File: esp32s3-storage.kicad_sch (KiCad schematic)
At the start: 27 parts, among them J1 USB_C_Receptacle_USB2.0_14P, J2 Conn_01x02, J3 Micro_SD_Card, J4 Conn_01x08_Socket, J5 Conn_01x15_Pin, J6 Conn_01x02_Pin, J7 Conn_01x03_Pin, Q1 CJ3401, SW1 SW_Push, SW2 SW_Push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

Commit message: begin modify pcb layout
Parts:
- F2: footprint Fuse:Fuse_0603_1608Metric -> Fuse:Fuse_0805_2012Metric
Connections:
- net SDHOST_CDET: now also U1.4 (IO4); no longer U1.10 (IO17)
- net SDHOST_CMD: now also U1.8 (IO15); no longer U1.6 (IO6)
- net SDHOST_DAT0: now also U1.6 (IO6); no longer U1.8 (IO15)
- net SDHOST_DAT1: now also U1.5 (IO5); no longer U1.9 (IO16)
- net SDHOST_DAT2: now also U1.10 (IO17); no longer U1.4 (IO4)
- net SDHOST_DAT3: now also U1.9 (IO16); no longer U1.5 (IO5)
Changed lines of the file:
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@@
 	)
 	(label "SDHOST_CMD"
-		(at 170.18 55.88 0)
+		(at 170.18 78.74 0)
 		(fields_autoplaced yes)
 		(effects
@@
 	)
 	(label "SDHOST_DAT0"
-		(at 170.18 78.74 0)
+		(at 170.18 55.88 0)
 		(fields_autoplaced yes)
 		(effects
@@
 	)
 	(label "SDHOST_DAT2"
-		(at 170.18 50.8 0)
+		(at 222.25 40.64 0)
 		(fields_autoplaced yes)
 		(effects
@@
 	)
 	(label "SDHOST_CDET"
-		(at 222.25 40.64 0)
+		(at 170.18 50.8 0)
 		(fields_autoplaced yes)
 		(effects
@@
 	)
 	(label "SDHOST_DAT1"
-		(at 170.18 81.28 0)
+		(at 170.18 53.34 0)
 		(fields_autoplaced yes)
 		(effects
@@
 	)
 	(label "SDHOST_DAT3"
-		(at 170.18 53.34 0)
+		(at 170.18 81.28 0)
 		(fields_autoplaced yes)
 		(effects
@@
 			)
 		)
-		(property "Footprint" "Fuse:Fuse_0603_1608Metric"
+		(property "Footprint" "Fuse:Fuse_0805_2012Metric"
 			(at 33.02 29.21 0)
 			(effects

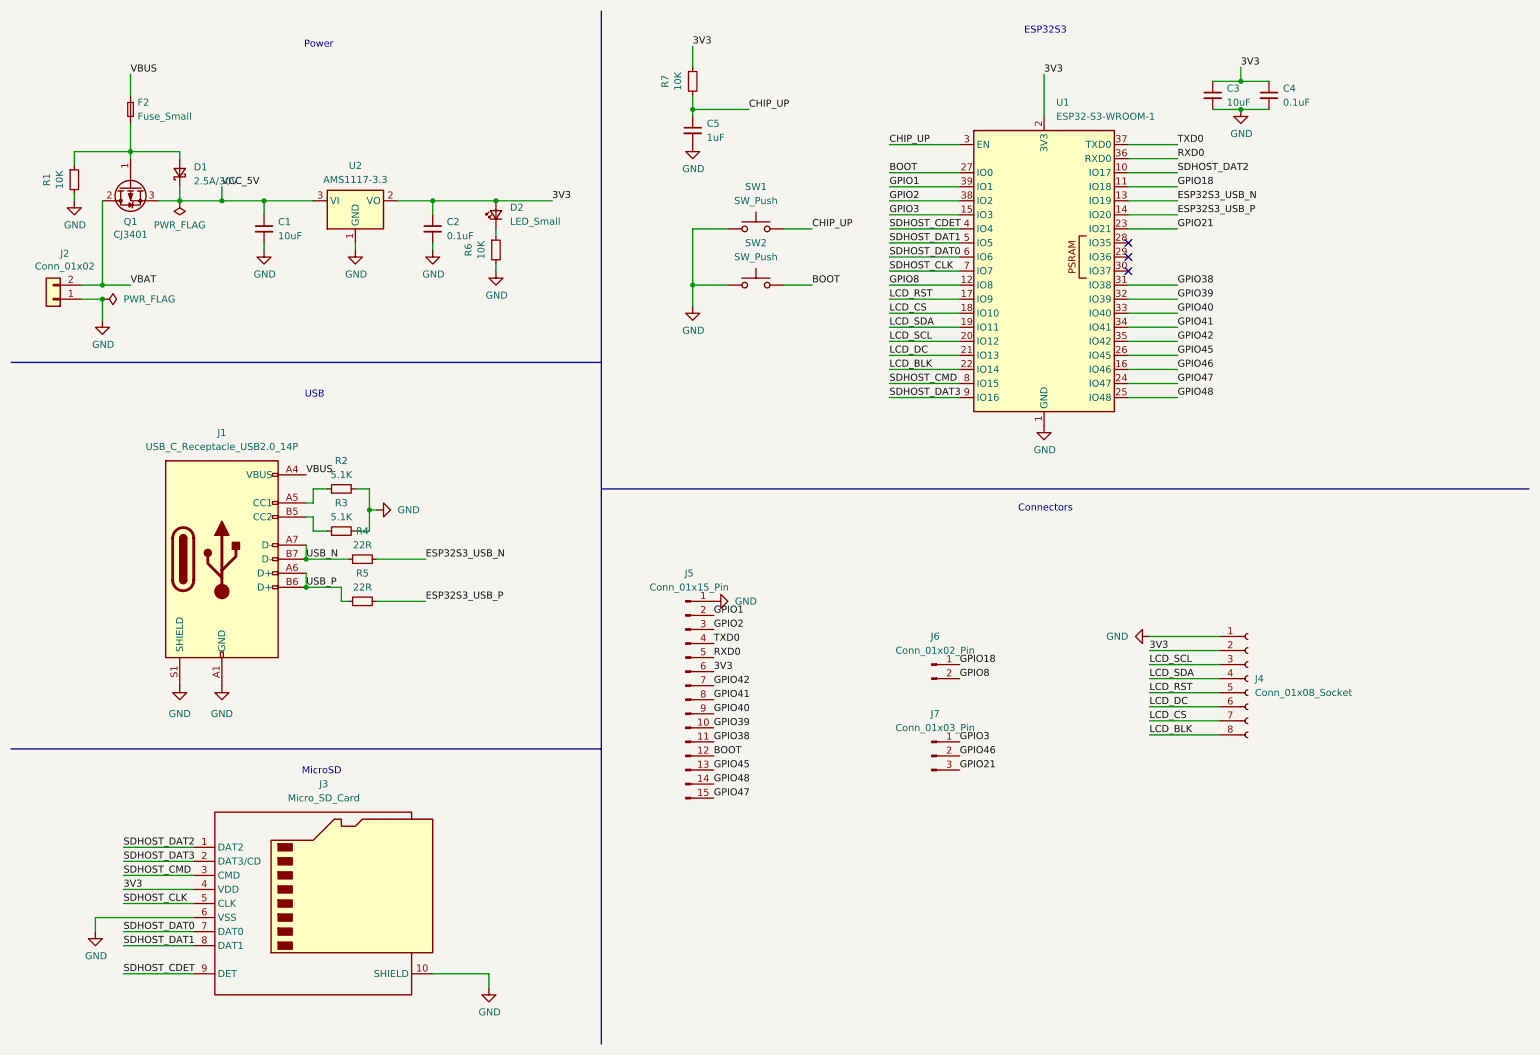
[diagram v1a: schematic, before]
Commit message: The second version of esp32s3 storage. Becare of the SDIO pins which are changed!
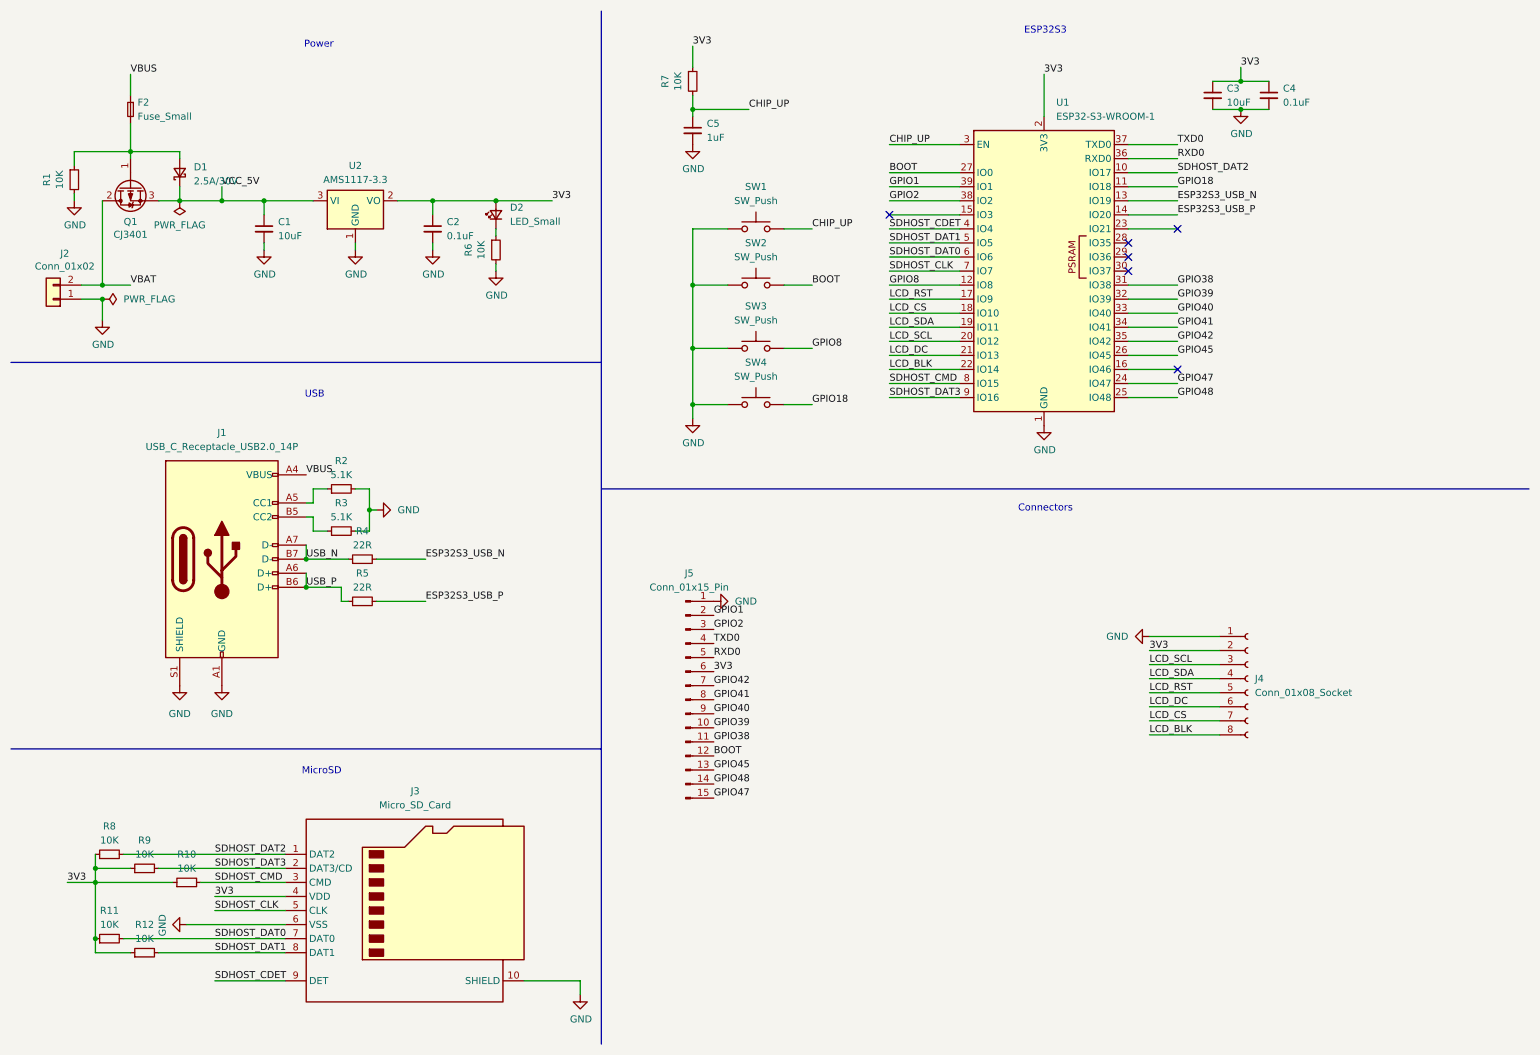
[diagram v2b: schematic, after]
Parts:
- removed J6: Conn_01x02_Pin, Connector_PinHeader_2.54mm:PinHeader_1x02_P2.54mm_Vertical, symbol Connector:Conn_01x02_Pin
- removed J7: Conn_01x03_Pin, Connector_PinHeader_2.54mm:PinHeader_1x03_P2.54mm_Vertical, symbol Connector:Conn_01x03_Pin
- added R10, R11, R12, R8, R9: 10K, Resistor_SMD:R_0603_1608Metric, symbol Device:R_Small
- added SW3, SW4: SW_Push, Button_Switch_SMD:SW_Push_1P1T_XKB_TS-1187A, symbol Switch:SW_Push
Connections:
- net 3V3: now also R10.1, R11.1, R12.1, R8.1, R9.1
- net GND: now also SW3.1, SW4.1
- net GPIO18: now also SW4.2
- net GPIO8: now also SW3.2
- net SDHOST_CMD: now also R10.2
- net SDHOST_DAT0: now also R11.2
- net SDHOST_DAT1: now also R12.2
- net SDHOST_DAT2: now also R8.2
- net SDHOST_DAT3: now also R9.2
- net GPIO21: no longer names the net of U1.23 (IO21)
- net GPIO3: no longer names the net of U1.15 (IO3)
- net GPIO46: no longer names the net of U1.16 (IO46)
- no-connect marks 3 -> 6
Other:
- moved on the sheet: J3

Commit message: esp32s3-storage v3
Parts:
- removed J4: Conn_01x08_Socket, Connector_PinSocket_2.54mm:PinSocket_1x08_P2.54mm_Vertical, symbol Connector:Conn_01x08_Socket
- removed J5: Conn_01x15_Pin, Connector_PinHeader_2.54mm:PinHeader_1x15_P2.54mm_Vertical, symbol Connector:Conn_01x15_Pin
- added C6: 0.1uF, Capacitor_SMD:C_0603_1608Metric, symbol Device:C_Small
- added J4: Conn_01x03_Pin, Connector_PinHeader_2.54mm:PinHeader_1x03_P2.54mm_Vertical, symbol Connector:Conn_01x03_Pin
- added J6: ~, user_created:fpc connector 1x12 P0.5mm bottom-side back-flip, symbol user_created:FPC_Connector_12_pin
- added Q2: SS8050, Package_TO_SOT_SMD:SOT-23, symbol Transistor_BJT:SS8050
- added R13: 10R, Resistor_SMD:R_0603_1608Metric, symbol Device:R_Small
- added R14: 1K, Resistor_SMD:R_0603_1608Metric, symbol Device:R_Small
- added R15: 10K, Resistor_SMD:R_0603_1608Metric, symbol Device:R_Small
- J2: footprint Connector_JST:JST_EH_S2B-EH_1x02_P2.50mm_Horizontal -> Connector_JST:JST_GH_SM02B-GHS-TB_1x02-1MP_P1.25mm_Horizontal
- SW1, SW2, SW3, SW4: footprint Button_Switch_SMD:SW_Push_1P1T_XKB_TS-1187A -> Button_Switch_SMD:SW_SPST_PTS647_Sx38
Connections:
- net 3V3: now also C6.2, J6.3 (LEDA), J6.4 (VDD), R15.1
- net GND: now also C6.1, J4.1 (Pin_1), J6.1 (GND), J6.12 (GND), J6.5 (GND), J6.6 (GND), Q2.2 (E)
- net LCD_BLK: now also R14.1
- net LCD_CS: now also J6.8 (CS)
- net LCD_DC: now also J6.7 (D/C)
- net LCD_RST: now also J6.11 (RESET)
- net LCD_SCL: now also J6.9 (SCL)
- net LCD_SDA: now also J6.10 (SDA)
- net RXD0: now also J4.3 (Pin_3)
- net TXD0: now also J4.2 (Pin_2)
- net GPIO3_S: now reaches U1.15 (IO3)
- net GPIO46_S: now reaches U1.16 (IO46)
- net GPIO21: now reaches U1.23 (IO21)
- net GPIO45 renamed GPIO45_S
- new net: Q2.1 (B), R14.2, R15.2
- new net: Q2.3 (C), R13.1
- new net LCD_LEDK: J6.2 (LEDK), R13.2
- no-connect marks 6 -> 3

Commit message: esp32s3-storage v4
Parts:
- J6: symbol user_created:FPC_Connector_12_pin -> user_created:FPC_Connector_bottom_12_pin
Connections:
- net GND: now also J6.13 (pad1), J6.14 (pad1)

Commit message: esp32s3-storage v5
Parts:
- C6: LCSC Part # C19702 -> C14663
- D1: LCSC Part # C82544 -> C8598
- J2: footprint Connector_JST:JST_GH_SM02B-GHS-TB_1x02-1MP_P1.25mm_Horizontal -> user_created:1x2 pin gap 1.25mm SMD socket; LCSC Part # (none) -> C2845379
- J3: LCSC Part # C113206 -> C381082
- J6: footprint user_created:fpc connector 1x12 P0.5mm bottom-side back-flip -> user_created:JST AFC01-S12FCC-00 1x2 P0.5mm back-flip bottom-side
- Q2: LCSC Part # (none) -> C2150
- R10, R11, R12, R15, R8, R9: LCSC Part # (none) -> C25804
- U1: LCSC Part # C2913198 -> C2913204
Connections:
- net GND: now also J2.2 (Pin_2), J2.3, J2.4; no longer J2.1 (Pin_1)
- net VBAT: now also J2.1 (Pin_1); no longer J2.2 (Pin_2)

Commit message: Add the sn for fpc socket
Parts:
- J6: LCSC Part # (none) -> C262268
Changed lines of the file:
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@@
+			)
+		)
+		(property "LCSC Part #" "C262268"
+			(at 267.97 134.62 0)
+			(effects
+				(font
+					(size 1.27 1.27)
+				)
+				(hide yes)
 			)
 		)

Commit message: add sn for fuse and type-c usb
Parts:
- F2: LCSC Part # C3161772 -> C7472578
- J1: LCSC Part # C2988369 -> C165948
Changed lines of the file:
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@@
 			)
 		)
-		(property "LCSC Part #" "C2988369"
+		(property "LCSC Part #" "C165948"
 			(at 49.53 110.49 0)
 			(effects
@@
 			)
 		)
-		(property "LCSC Part #" "C3161772"
+		(property "LCSC Part #" "C7472578"
 			(at 33.02 29.21 0)
 			(effects
